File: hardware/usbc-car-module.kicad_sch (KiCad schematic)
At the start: 0 parts

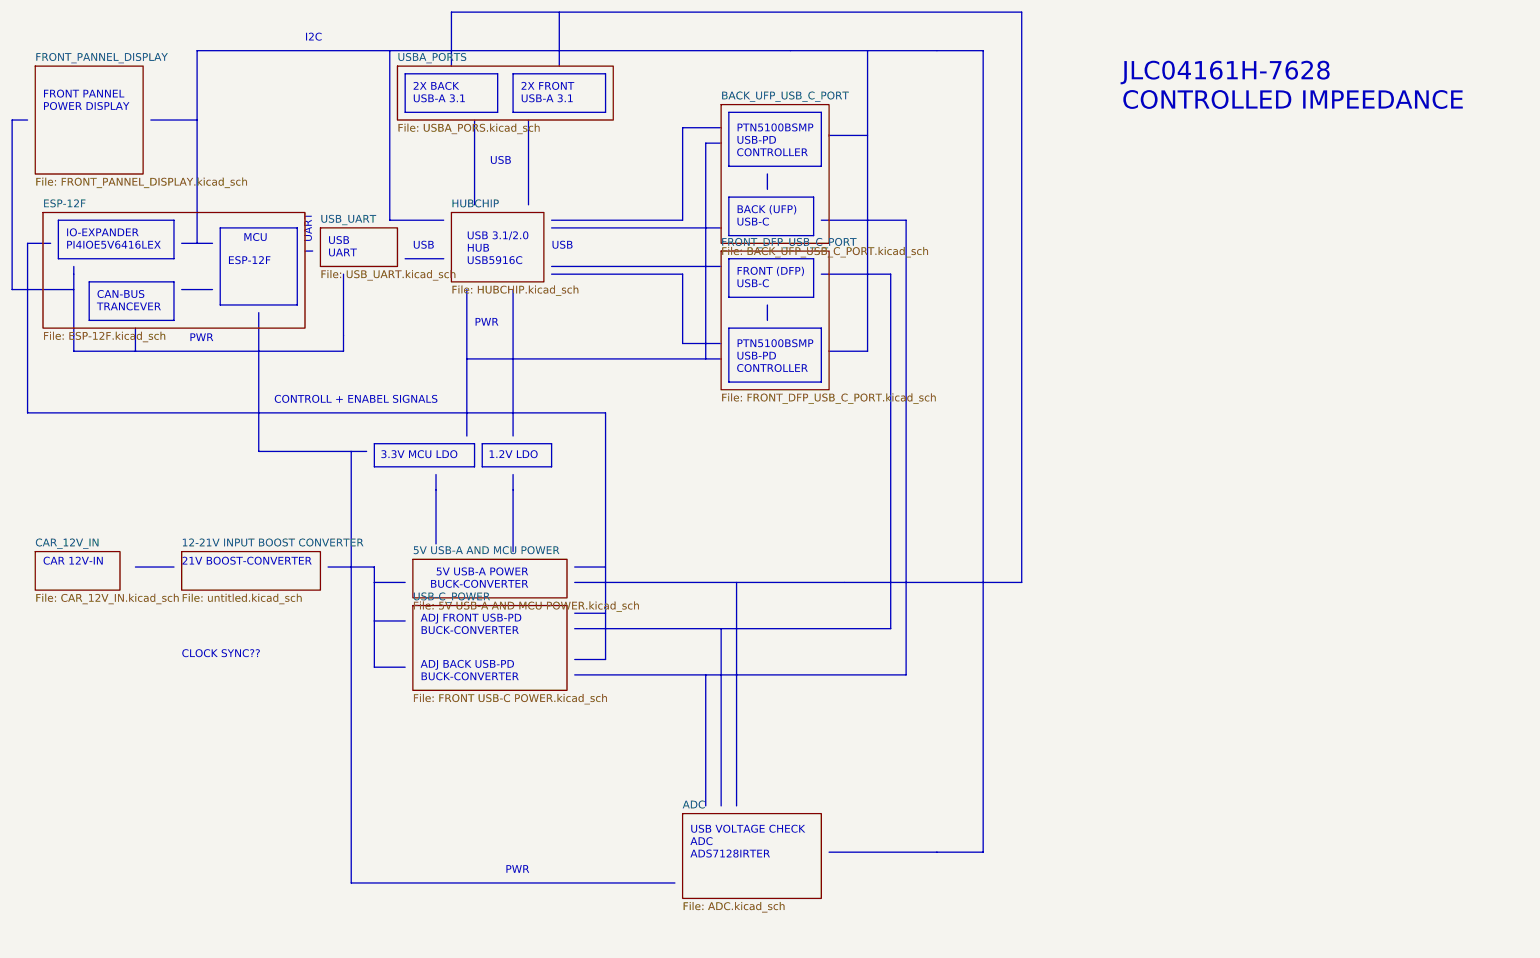
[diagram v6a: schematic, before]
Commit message: updated block digram minor pcb changes
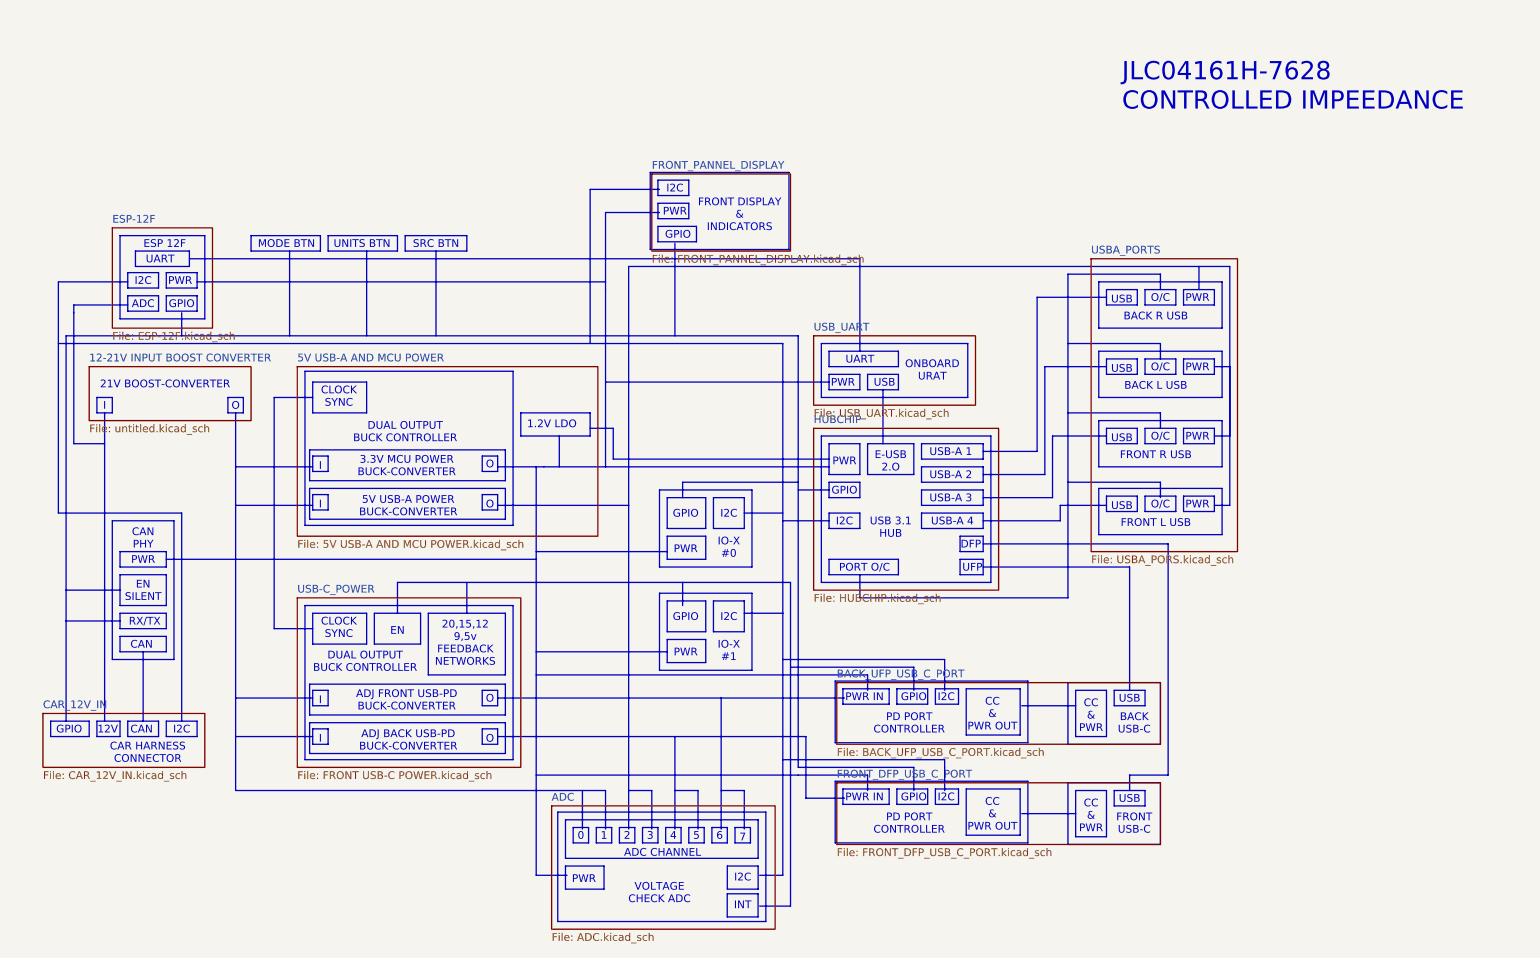
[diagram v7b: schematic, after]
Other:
- note added: "0"
- note added: "1"
- note added: "12V"
- note added: "2"
- note added: "20,15,12 9,5v FEEDBACK NETWORKS"
- note added: "3"
- note added: "3.3V MCU POWER BUCK-CONVERTER"
- note added: "4"
- note added: "5"
- note added: "6"
- note added: "7"
- note added: "ADC"
- note added: "ADC CHANNEL"
- note added: "BACK L USB"
- note added: "BACK R USB"
- note added: "BACK USB-C"
- note added: "CAN"
- note added: "CAN PHY"
- note added: "CAR HARNESS CONNECTOR"
- note added: "CC & PWR"
- note added: "CC & PWR OUT"
- note added: "CLOCK SYNC"
- note added: "DFP"
- note added: "DUAL OUTPUT BUCK CONTROLLER"
- note added: "E-USB 2.O"
- note added: "EN"
- note added: "EN SILENT"
- note added: "ESP 12F"
- note added: "FRONT DISPLAY & INDICATORS"
- note added: "FRONT L USB"
- note added: "FRONT R USB"
- note added: "FRONT USB-C"
- note added: "GPIO"
- note added: "I"
- note added: "INT"
- note added: "IO-X #0"
- note added: "IO-X #1"
- note added: "MODE BTN"
- note added: "O"
- note added: "O/C"
- note added: "ONBOARD URAT"
- note added: "PD PORT CONTROLLER"
- note added: "PORT O/C"
- note added: "PWR IN"
- note added: "RX/TX"
- note added: "SRC BTN"
- note added: "UFP"
- note added: "UNITS BTN"
- note added: "USB 3.1 HUB"
- note added: "USB-A 1"
- note added: "USB-A 2"
- note added: "USB-A 3"
- note added: "USB-A 4"
- note added: "VOLTAGE CHECK ADC"
- note removed: "2X BACK USB-A 3.1"
- note removed: "2X FRONT USB-A 3.1"
- note removed: "BACK (UFP) USB-C"
- note removed: "CAN-BUS TRANCEVER"
- note removed: "CAR 12V-IN"
- note removed: "CLOCK SYNC??"
- note removed: "CONTROLL + ENABEL SIGNALS"
- note removed: "ESP-12F"
- note removed: "FRONT (DFP) USB-C"
- note removed: "FRONT PANNEL POWER DISPLAY"
- note removed: "IO-EXPANDER PI4IOE5V6416LEX"
- note removed: "MCU"
- note removed: "PTN5100BSMP USB-PD CONTROLLER"
- note removed: "USB 3.1/2.0 HUB USB5916C"
- note removed: "USB UART"
- note removed: "USB VOLTAGE CHECK ADC ADS7128IRTER"
